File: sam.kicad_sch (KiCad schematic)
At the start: 56 parts, among them IC1 HYB4116, IC15 MC6883, IC16 74LS244N, IC2 HYB4116, IC3 HYB4116, IC31 74LS02N, IC33 74LS138N, IC4 HYB4116, IC5 HYB4116, IC6 HYB4116, IC7 HYB4116, IC8 HYB4116

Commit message: work on memory sub system
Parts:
- removed C10, C11, C12, C13, C14, C2, C24, C3, C5, C6, C7, C8, C9: 0.1uF, Capacitor_THT:C_Disc_D4.3mm_W1.9mm_P5.00mm, symbol Device:C_Small
- removed C21, C26: 4.7uF, Capacitor_THT:CP_Radial_D5.0mm_P2.50mm, symbol Device:C_Polarized_Small
- removed C25: 10uF, Capacitor_THT:CP_Radial_D5.0mm_P2.50mm, symbol Device:C_Polarized_Small
- removed C27: 0.01uF, Capacitor_THT:C_Disc_D4.3mm_W1.9mm_P5.00mm, symbol Device:C_Small
- removed C59: 33pF, Capacitor_THT:C_Disc_D4.3mm_W1.9mm_P5.00mm, symbol Device:C_Small
- removed IC2, IC3, IC4, IC5, IC6, IC7, IC8: HYB4116, Package_DIP:DIP-16_W7.62mm, symbol Memory_RAM_Siemens:HYB4116
- removed JP1-1: 1 low, Connector_PinHeader_2.54mm:PinHeader_1x03_P2.54mm_Vertical, symbol Jumper:Jumper_3_Bridged12
- removed JP3-1, JP5-1, JP7-1: 16k/32k, Connector_PinHeader_2.54mm:PinHeader_1x03_P2.54mm_Vertical, symbol Jumper:Jumper_3_Bridged12
- removed R17: 1K5, Resistor_THT:R_Axial_DIN0309_L9.0mm_D3.2mm_P12.70mm_Horizontal, symbol Device:R_Small
- added C16, C19, C20, C21, C51: 0.1uF, Capacitor_THT:C_Disc_D4.3mm_W1.9mm_P5.00mm, symbol Device:C_Small
- added IC2, IC3, IC4, IC5, IC6, IC7, IC8: M3732H-20RS, Package_DIP:DIP-16_W7.62mm, symbol vdg:MSM3732
- added LK2: LK2, Connector_PinHeader_2.54mm:PinHeader_1x03_P2.54mm_Vertical, symbol Jumper:Jumper_3_Bridged12
- C37: footprint Capacitor_THT:CP_Radial_D5.0mm_P2.50mm -> Capacitor_THT:CP_Radial_Tantal_D5.5mm_P5.00mm
- C40: footprint Capacitor_THT:C_Disc_D4.3mm_W1.9mm_P5.00mm -> Dragon:C_Radial_Special
- C41: footprint Capacitor_THT:C_Disc_D4.3mm_W1.9mm_P5.00mm -> Capacitor_THT:C_Disc_D3.0mm_W1.6mm_P2.50mm
- IC1: value HYB4116 -> M3732H-20RS; symbol Memory_RAM_Siemens:HYB4116 -> vdg:MSM3732
- R12: renamed from R4; footprint Resistor_THT:R_Axial_DIN0309_L9.0mm_D3.2mm_P12.70mm_Horizontal -> Dragon:R_Axial_DIN0309_L9.0mm_D2.5mm_P12.70mm_Horizontal
- R19, R20, R21, R22, R23, R24, R25, R28: footprint Resistor_THT:R_Axial_DIN0309_L9.0mm_D3.2mm_P12.70mm_Horizontal -> Dragon:R_Axial_DIN0309_L9.0mm_D2.5mm_P12.70mm_Horizontal
- R26: renamed from R27; footprint Resistor_THT:R_Axial_DIN0309_L9.0mm_D3.2mm_P12.70mm_Horizontal -> Dragon:R_Axial_DIN0309_L9.0mm_D2.5mm_P12.70mm_Horizontal
- R27: renamed from R26; footprint Resistor_THT:R_Axial_DIN0309_L9.0mm_D3.2mm_P12.70mm_Horizontal -> Dragon:R_Axial_DIN0309_L9.0mm_D2.5mm_P12.70mm_Horizontal
- R37: renamed from R3; footprint Resistor_THT:R_Axial_DIN0309_L9.0mm_D3.2mm_P12.70mm_Horizontal -> Dragon:R_Axial_DIN0309_L9.0mm_D2.5mm_P12.70mm_Horizontal
- R39: renamed from R2; footprint Resistor_THT:R_Axial_DIN0309_L9.0mm_D3.2mm_P12.70mm_Horizontal -> Dragon:R_Axial_DIN0309_L9.0mm_D2.5mm_P12.70mm_Horizontal
- renumbered C16 to C14
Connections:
- net +5V: now also R39.1, C51.2; no longer R39.2
- net D0: now also IC8.2 (Din)
- net D1: now also IC7.2 (Din)
- net D2: now also IC6.2 (Din)
- net D3: now also IC5.2 (Din)
- net D4: now also IC4.2 (Din)
- net D5: now also IC3.2 (Din)
- net D6: now also IC2.2 (Din)
- net DO0: now also IC8.14 (Dout)
- net DO1: now also IC7.14 (Dout)
- net DO2: now also IC6.14 (Dout)
- net DO3: now also IC5.14 (Dout)
- net DO4: now also IC4.14 (Dout)
- net DO5: now also IC3.14 (Dout)
- net DO6: now also IC2.14 (Dout)
- net EXTMEN: now also R39.2; no longer R39.1
- net GND: now also C14.2, C15.2, C41.2, C16.2, C19.2, C20.2, C21.2, C51.1, IC2.16 (VSS), IC3.16 (VSS), IC4.16 (VSS), IC5.16 (VSS), IC6.16 (VSS), IC7.16 (VSS), IC8.16 (VSS); no longer C14.1, C15.1, C41.1
- net RAM VCC: now also C14.1, C15.1, C17.1, C18.1, IC1.8 (VCC), C16.1, C19.1, C20.1, C21.1, IC2.8 (VCC), IC3.8 (VCC), IC4.8 (VCC), IC5.8 (VCC), IC6.8 (VCC), IC7.8 (VCC), IC8.8 (VCC); no longer IC1.9 (VCC)
- net R/~{W}: now also IC31.8; no longer IC31.2
- net S2: now also IC31.9; no longer IC31.3
- net Z0: now also IC2.5 (A0), IC3.5 (A0), IC4.5 (A0), IC5.5 (A0), IC6.5 (A0), IC7.5 (A0), IC8.5 (A0)
- net Z1: now also R23.1, IC2.7 (A1), IC3.7 (A1), IC4.7 (A1), IC5.7 (A1), IC6.7 (A1), IC7.7 (A1), IC8.7 (A1); no longer R24.1
- net Z2: now also R24.1, IC2.6 (A2), IC3.6 (A2), IC4.6 (A2), IC5.6 (A2), IC6.6 (A2), IC7.6 (A2), IC8.6 (A2); no longer R23.1
- net Z3: now also IC2.12 (A3), IC3.12 (A3), IC4.12 (A3), IC5.12 (A3), IC6.12 (A3), IC7.12 (A3), IC8.12 (A3)
- net Z4: now also IC2.11 (A4), IC3.11 (A4), IC4.11 (A4), IC5.11 (A4), IC6.11 (A4), IC7.11 (A4), IC8.11 (A4)
- net Z5: now also IC2.10 (A5), IC3.10 (A5), IC4.10 (A5), IC5.10 (A5), IC6.10 (A5), IC7.10 (A5), IC8.10 (A5)
- net Z6: now also IC2.13 (A6), IC3.13 (A6), IC4.13 (A6), IC5.13 (A6), IC6.13 (A6), IC7.13 (A6), IC8.13 (A6)
- net Z7: now also IC31.2, IC31.3, LK2.1 (A); no longer IC31.5, IC31.6
- net ~{CAS}: now also IC2.15 (~{CAS}), IC3.15 (~{CAS}), IC4.15 (~{CAS}), IC5.15 (~{CAS}), IC6.15 (~{CAS}), IC7.15 (~{CAS}), IC8.15 (~{CAS})
- net ~{RAS0}: now also IC2.4 (~{RAS}), IC3.4 (~{RAS}), IC4.4 (~{RAS}), IC5.4 (~{RAS}), IC6.4 (~{RAS}), IC7.4 (~{RAS}), IC8.4 (~{RAS})
- net ~{WE}: now also IC2.3 (~{WE}), IC3.3 (~{WE}), IC4.3 (~{WE}), IC5.3 (~{WE}), IC6.3 (~{WE}), IC7.3 (~{WE}), IC8.3 (~{WE})
- net nZ7: now reaches R12.1
- net nZ7: now also IC1.9 (A7), IC2.9 (A7), IC3.9 (A7), IC4.9 (A7), IC5.9 (A7), IC6.9 (A7), IC7.9 (A7), IC8.9 (A7)
- net at C40.2, IC15.5 (OSCIN): now also XL2.2; no longer XL2.1
- net at R37.1: now also C41.1, XL2.1; no longer IC15.6 (OSCOUT)
- net at IC33.5 (E2): now also IC31.10; no longer IC31.1
- removed net RAM VBB: C17.1, C18.1, IC1.1 (VBB)
- removed net RAM VDD: C14.2, C15.2, IC1.8 (VDD)
- new net: IC15.6 (OSCOUT), R37.2
- new net: IC31.1, LK2.3 (B)
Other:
- moved on the sheet: C14, C41, R37, R39

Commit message: add PIA and VDG to schematics
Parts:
- IC31: SA2120 Sheet 1 -> (none)
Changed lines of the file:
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@@
 			)
 		)
-		(property "SA2120" "Sheet 1"
-			(at 219.964 125.222 0)
-			(effects
-				(font
-					(size 1.27 1.27)
-				)
-				(hide yes)
-			)
-		)
 		(pin "1"
 		)
@@
 			)
 		)
-		(property "SA2120" "Sheet 1"
-			(at 96.901 166.37 0)
-			(effects
-				(font
-					(size 1.27 1.27)
-				)
-				(hide yes)
-			)
-		)
 		(pin "1"
 		)
@@
 			(at 95.25 185.42 0)
 			(effects
-				(font
-					(size 1.27 1.27)
-				)
-				(hide yes)
-			)
-		)
-		(property "SA2120" "Sheet 1"
-			(at 95.25 185.42 0)
-			(effects

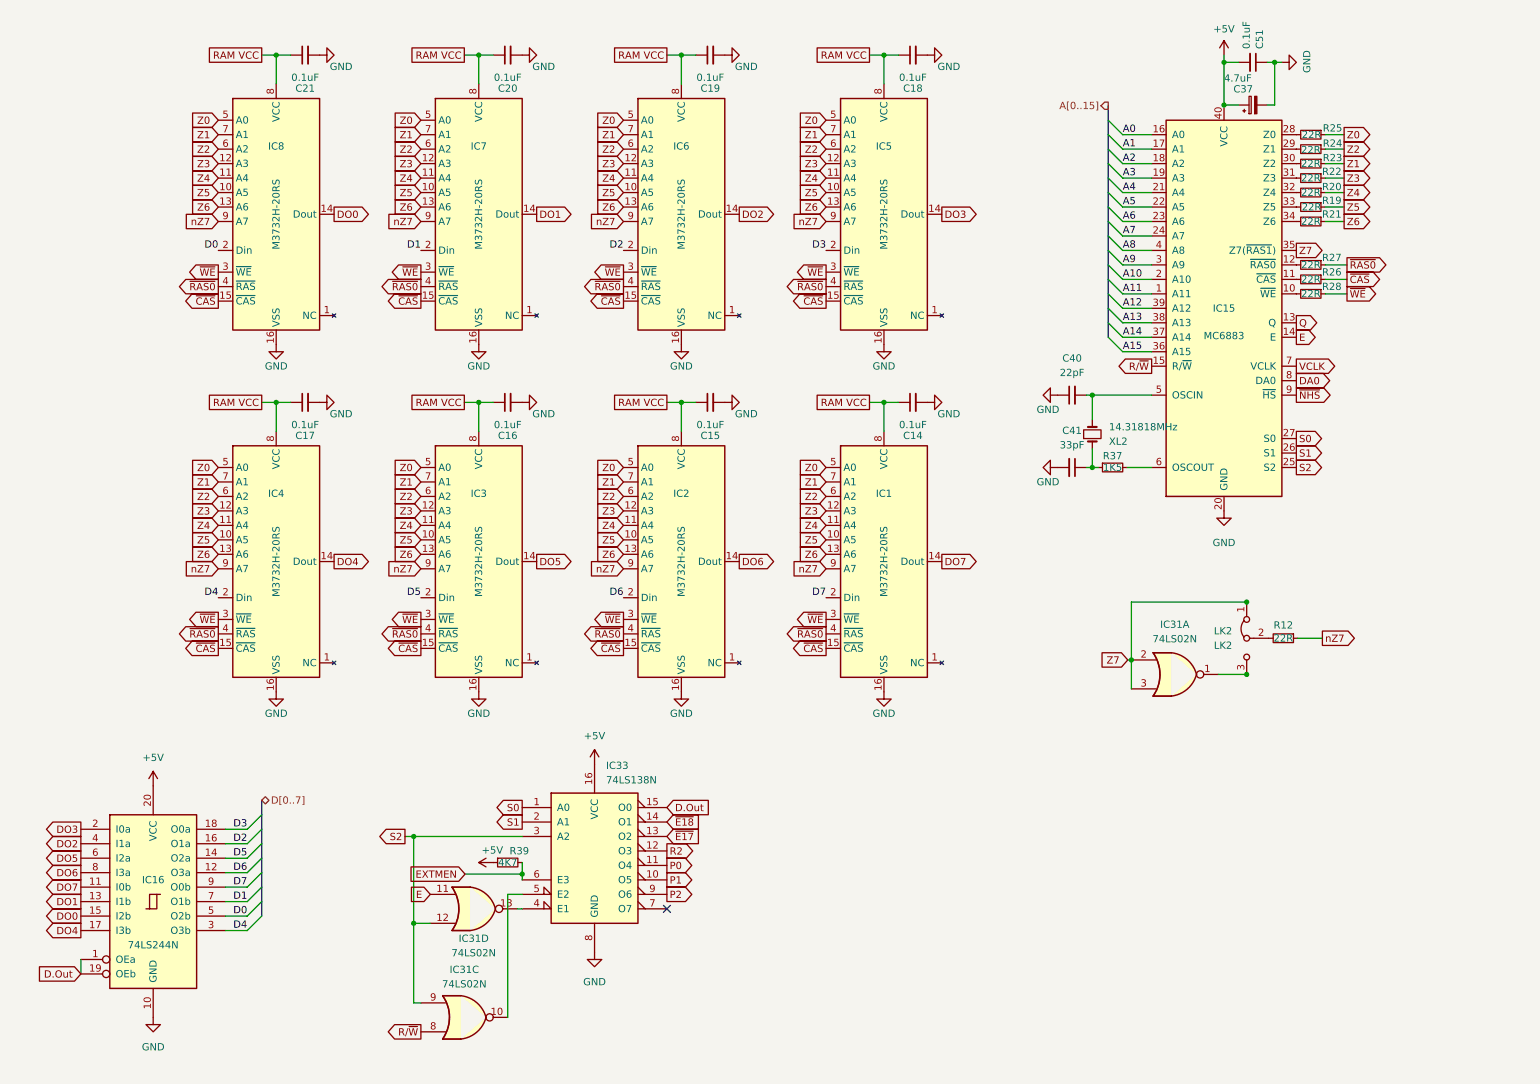
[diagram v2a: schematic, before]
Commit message: add video padding circuit
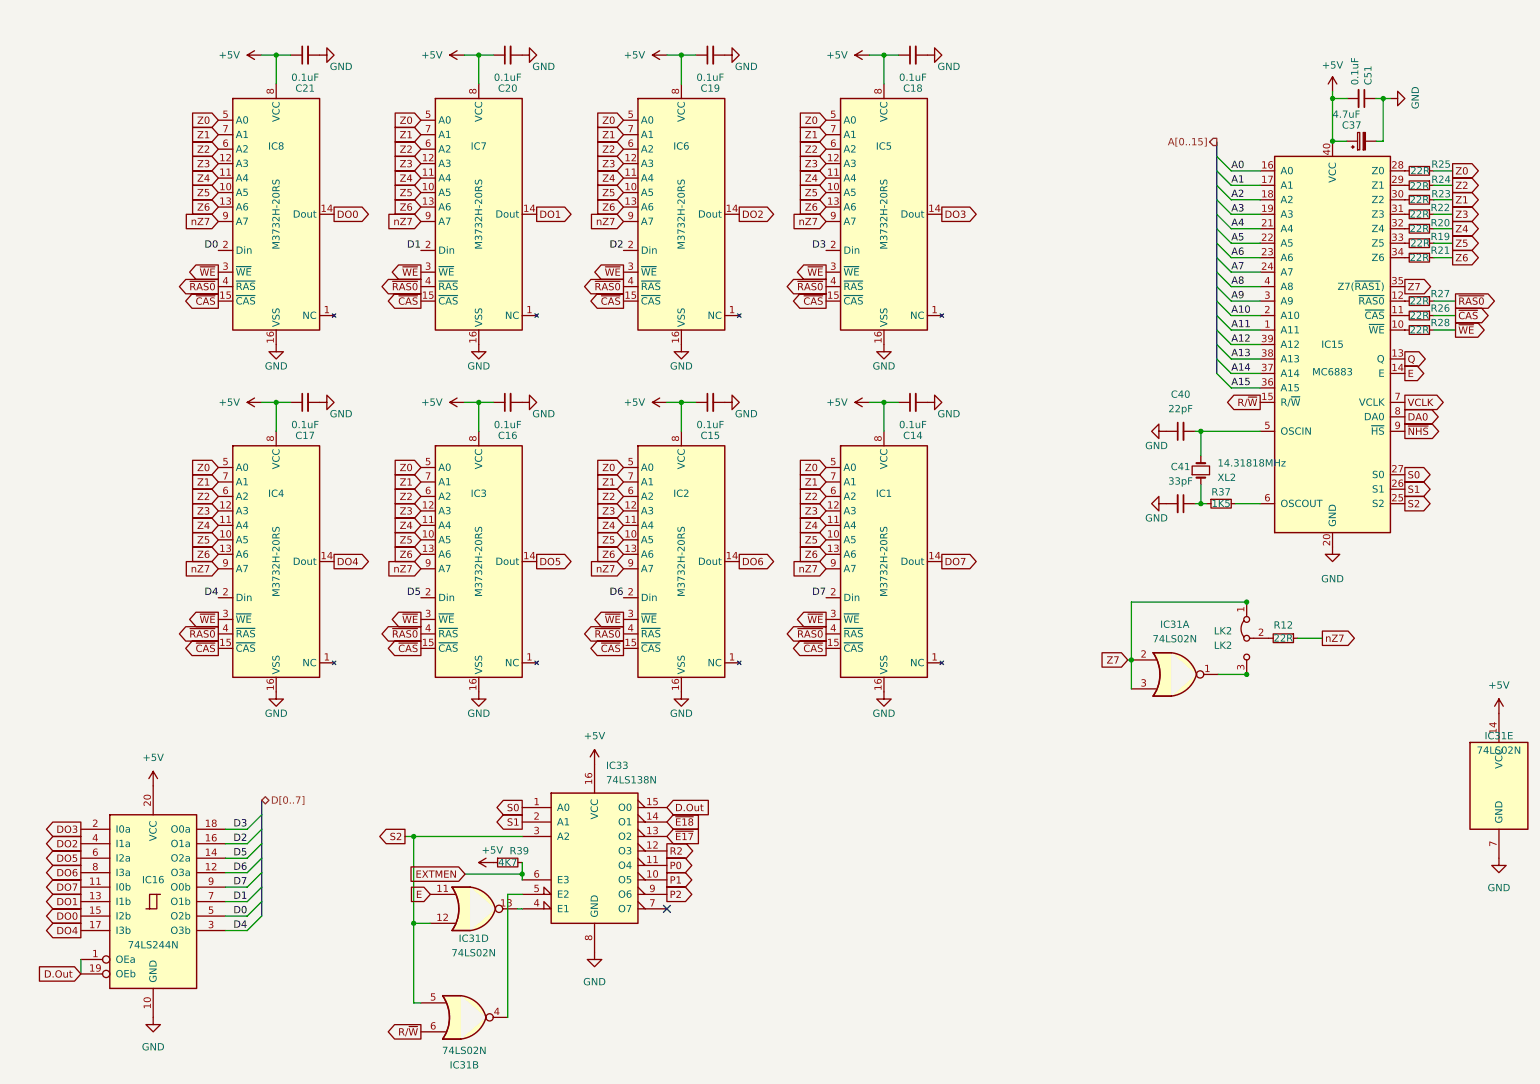
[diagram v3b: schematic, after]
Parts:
- added unit 5 of IC31
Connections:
- net RAM VCC is gone; now on net +5V: C14.1, C15.1, C16.1, C17.1, C18.1, C19.1, C20.1, C21.1, IC1.8 (VCC), IC2.8 (VCC), IC3.8 (VCC), IC4.8 (VCC), IC5.8 (VCC), IC6.8 (VCC), IC7.8 (VCC), IC8.8 (VCC)
- net +5V: now also IC31.14 (VCC)
- net GND: now also IC31.7 (GND)
- net R/~{W}: now also IC31.6; no longer IC31.8
- net S2: now also IC31.5; no longer IC31.9
- net at IC33.5 (E2): now also IC31.4; no longer IC31.10
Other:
- moved on the sheet: C37, C40, C41, C51, IC15, R19, R20, R21, R22, R23, R24, R25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

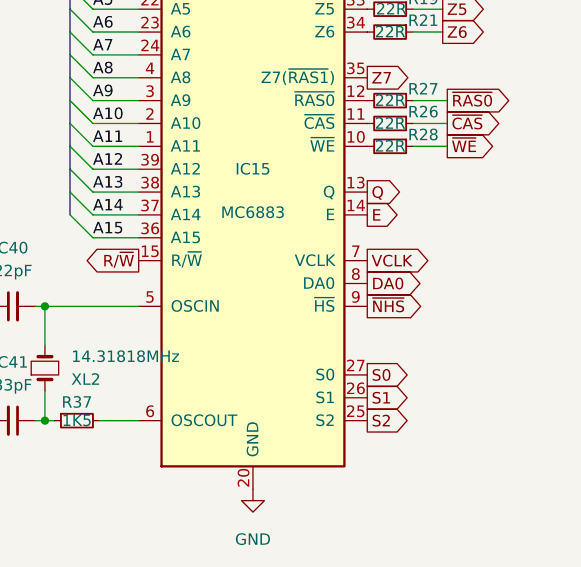
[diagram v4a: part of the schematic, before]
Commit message: FM generator routing
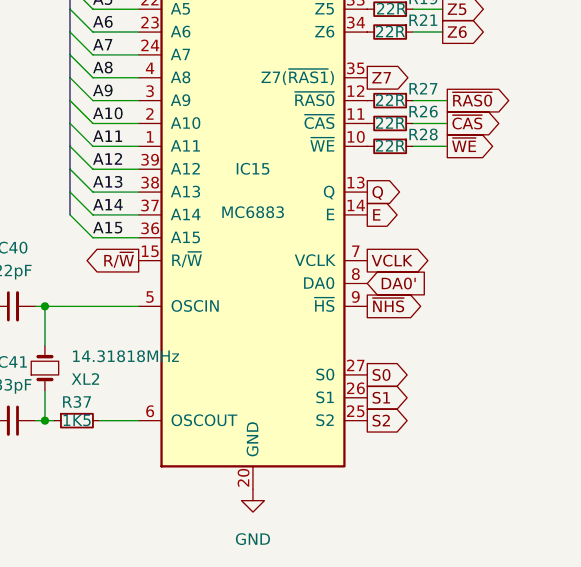
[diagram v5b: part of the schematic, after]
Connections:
- net DA0 renamed DA0'

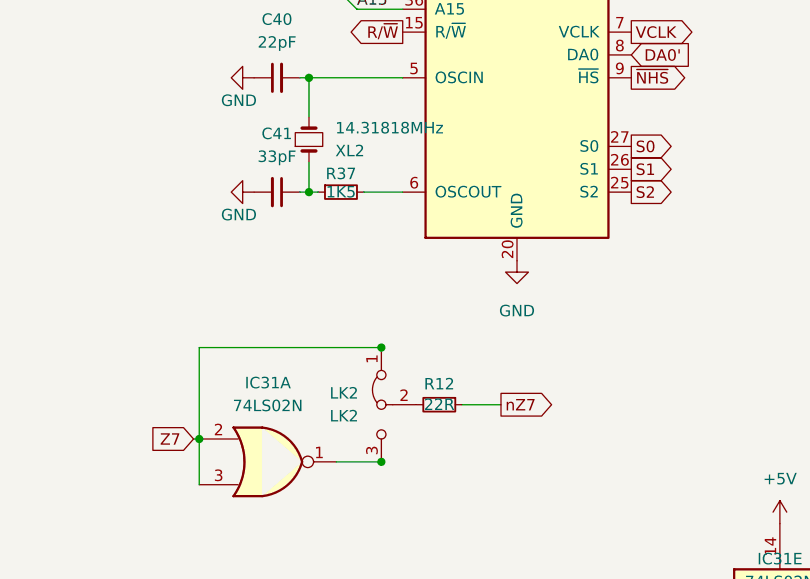
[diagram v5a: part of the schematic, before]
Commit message: resolve missing connections
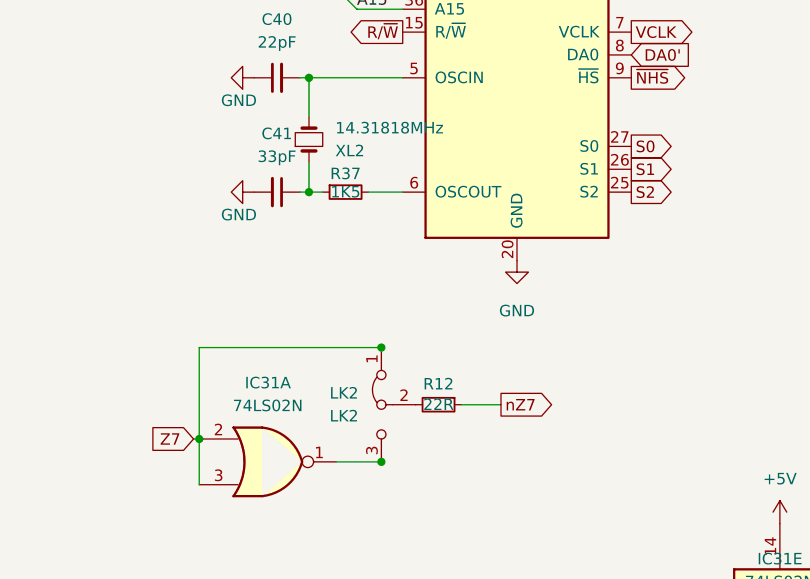
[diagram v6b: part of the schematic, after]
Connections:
- net at R12.2: now also LK2.2 (C)
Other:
- moved on the sheet: R37
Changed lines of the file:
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@@
 	(wire
 		(pts
-			(xy 224.536 95.25) (xy 225.552 95.25)
+			(xy 224.536 95.25) (xy 226.06 95.25)
 		)
 		(stroke
@@
 	(wire
 		(pts
-			(xy 230.632 95.25) (xy 234.95 95.25)
+			(xy 231.14 95.25) (xy 234.95 95.25)
 		)
 		(stroke
@@
 	(wire
 		(pts
-			(xy 245.872 118.872) (xy 241.554 118.872)
+			(xy 245.872 118.872) (xy 241.4701 118.872)
 		)
 		(stroke
@@
 	(symbol
 		(lib_id "Device:R_Small")
-		(at 228.092 95.25 90)
+		(at 228.6 95.25 90)
 		(mirror x)
 		(unit 1)
@@
 		(dnp no)
 		(property "Reference" "R37"
-			(at 228.092 93.218 90)
+			(at 228.6 93.218 90)
 			(effects
 				(font
@@
 		)
 		(property "Value" "1K5"
-			(at 228.092 95.25 90)
+			(at 228.6 95.25 90)
 			(effects
 				(font
@@
 		)
 		(property "Footprint" "Dragon:R_Axial_DIN0309_L9.0mm_D2.5mm_P12.70mm_Horizontal"
-			(at 228.092 95.25 0)
+			(at 228.6 95.25 0)
 			(effects
 				(font
@@
 		)
 		(property "Datasheet" "~"
-			(at 228.092 95.25 0)
+			(at 228.6 95.25 0)
 			(effects
 				(font
@@
 		)
 		(property "Description" ""
-			(at 228.092 95.25 0)
+			(at 228.6 95.25 0)
 			(effects
 				(font
@@
 		)
 		(property "DigiKey" "CF14JT1K50CT-ND"
-			(at 228.092 95.25 0)
+			(at 228.6 95.25 0)
 			(effects
 				(font
@@
 	(symbol
 		(lib_id "Device:R_Small")
-		(at 239.014 118.872 270)
+		(at 238.9301 118.872 270)
 		(unit 1)
 		(exclude_from_sim no)
@@
 		(dnp no)
 		(property "Reference" "R12"
-			(at 239.014 116.586 90)
+			(at 238.9301 116.586 90)
 			(effects
 				(font
@@
 		)
 		(property "Value" "22R"
-			(at 239.014 118.872 90)
+			(at 238.9301 118.872 90)
 			(effects
 				(font
@@
 		)
 		(property "Footprint" "Dragon:R_Axial_DIN0309_L9.0mm_D2.5mm_P12.70mm_Horizontal"
-			(at 239.014 118.872 0)
+			(at 238.9301 118.872 0)
 			(effects
 				(font
@@
 		)
 		(property "Datasheet" "~"
-			(at 239.014 118.872 0)
+			(at 238.9301 118.872 0)
 			(effects
 				(font
@@
 		)
 		(property "Description" ""
-			(at 239.014 118.872 0)
+			(at 238.9301 118.872 0)
 			(effects
 				(font
@@
 		)
 		(property "DigiKey" "CF14JT22R0CT-ND"
-			(at 239.014 118.872 0)
+			(at 238.9301 118.872 0)
 			(effects
 				(font
